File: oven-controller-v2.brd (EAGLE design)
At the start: 160 x 100 mm, 28 parts, among them Q1 IRFL310, Q2 IRFL310, U1 ARDUINO_SHIELDLONGPADS

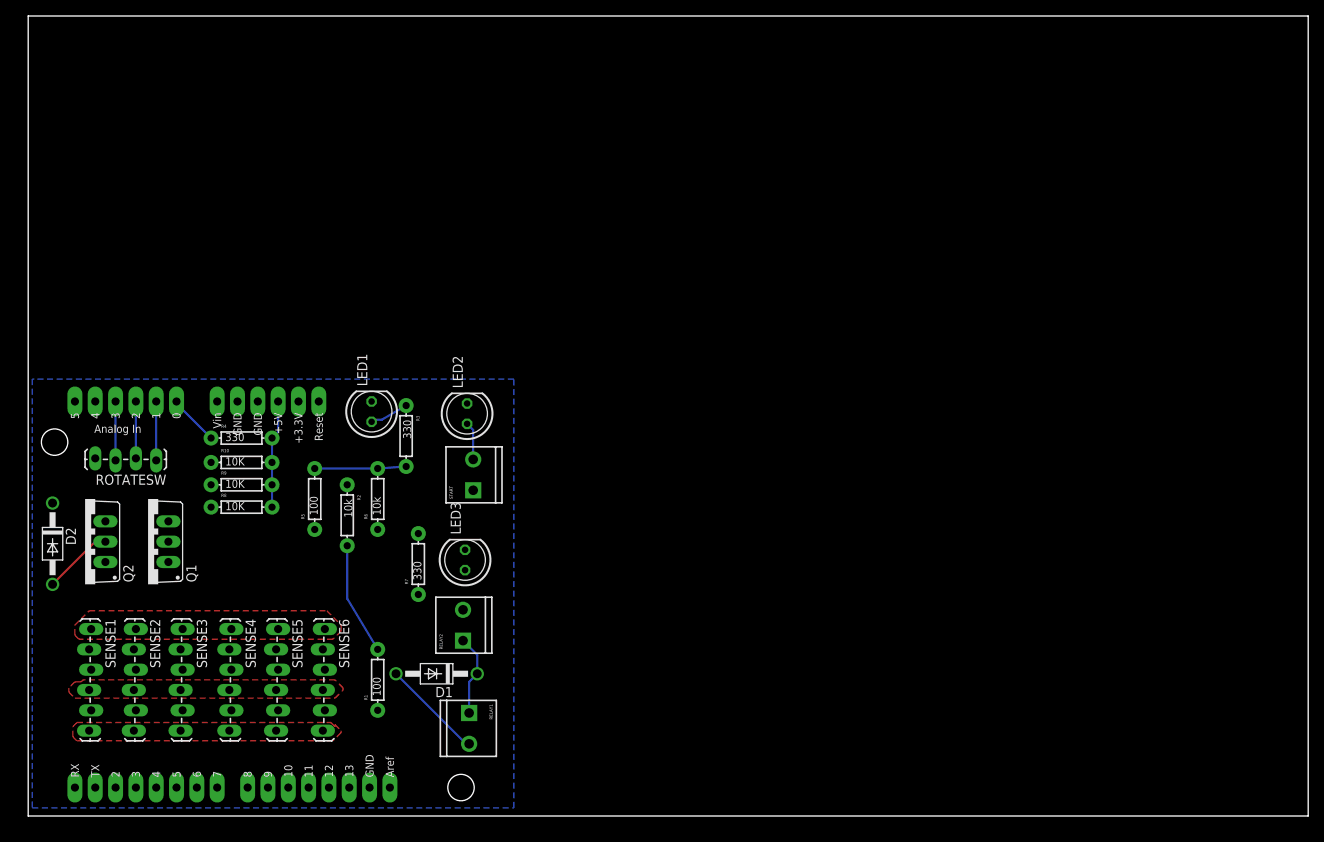
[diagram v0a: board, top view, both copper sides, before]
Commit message: Laid out board for v2. ERC and DRC good. Generated Gerbers.
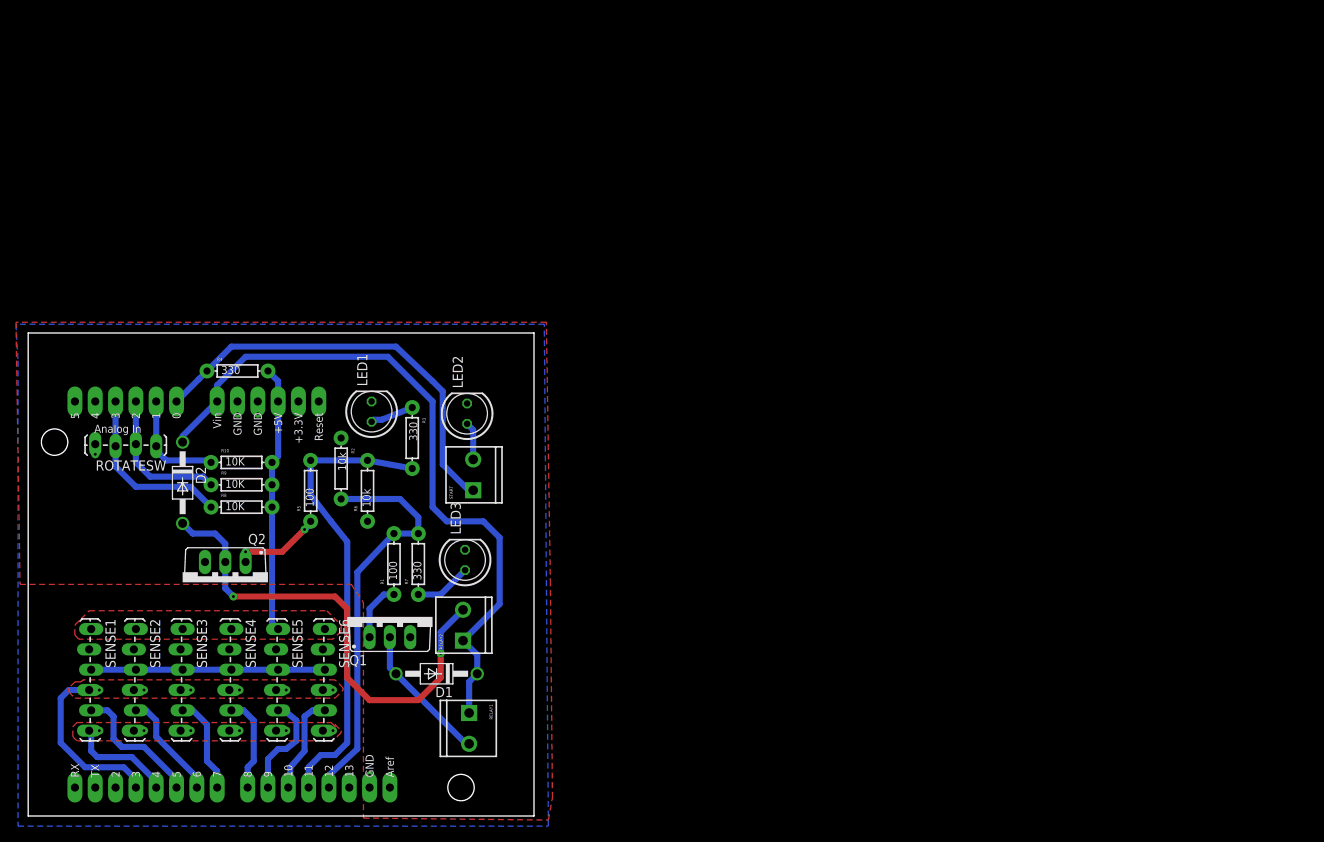
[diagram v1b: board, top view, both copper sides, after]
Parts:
- moved Q1 31.7 mm to (45.2, 24.9), turned to 0 degrees
- moved Q2 18.2 mm to (24.6, 29.2), turned to 180 degrees
- moved D2 18.0 mm to (19.3, 41.7)
- moved R1 14.6 mm to (45.7, 31.5)
- moved R4 8.40 mm to (26.2, 55.6)
- moved R2 5.89 mm to (39.1, 43.4)
- moved ROTATESW 1.78 mm to (16.0, 46.2)
- moved R6 1.63 mm to (42.4, 40.6)
- moved R5 1.14 mm to (35.3, 40.6)
- moved R3 0.80 mm to (48.0, 47.2)
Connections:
- net SDA_PIN3 renamed CCO
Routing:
- net VIN: track 10.2 -> 87.8 mm
- net N$4: track 8.81 -> 60.6 mm, vias 0 -> 2
- net CS_PIN11: track 11.4 -> 58.3 mm
- net A0: track 6.36 -> 52.9 mm
- net CS_PIN12: track 14.0 -> 50.8 mm
- net GND: track 0.00 -> 29.2 mm, vias 0 -> 4
- net CCO: track 0.00 -> 21.9 mm, vias 0 -> 6
- net 5V: track 13.5 -> 33.4 mm
- net CS_PIN5: track 0.00 -> 16.9 mm
- net A3: track 7.37 -> 22.2 mm
- net CS_PIN6: track 0.00 -> 13.6 mm
- net CS_PIN9: track 0.00 -> 13.3 mm
- net SCLK_PIN4: track 0.00 -> 13.1 mm, vias 0 -> 6
- net CS_PIN10: track 0.00 -> 12.5 mm
- net CS_PIN7: track 0.00 -> 12.2 mm
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- added copper zone on layer 1, net GND
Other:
- board size 160 x 100 mm -> 63.2 x 60.4 mm
